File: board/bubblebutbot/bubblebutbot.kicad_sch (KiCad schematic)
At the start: 15 parts, among them J1 Screw_Terminal_01x02, J2 Screw_Terminal_01x02, J3 Conn_01x06_Female, J4 Conn_01x06_Female, Q1 FDN336P, U1 WeMos_D1_mini, U2 18350-HOLDER, U3 TPS613222ADBV

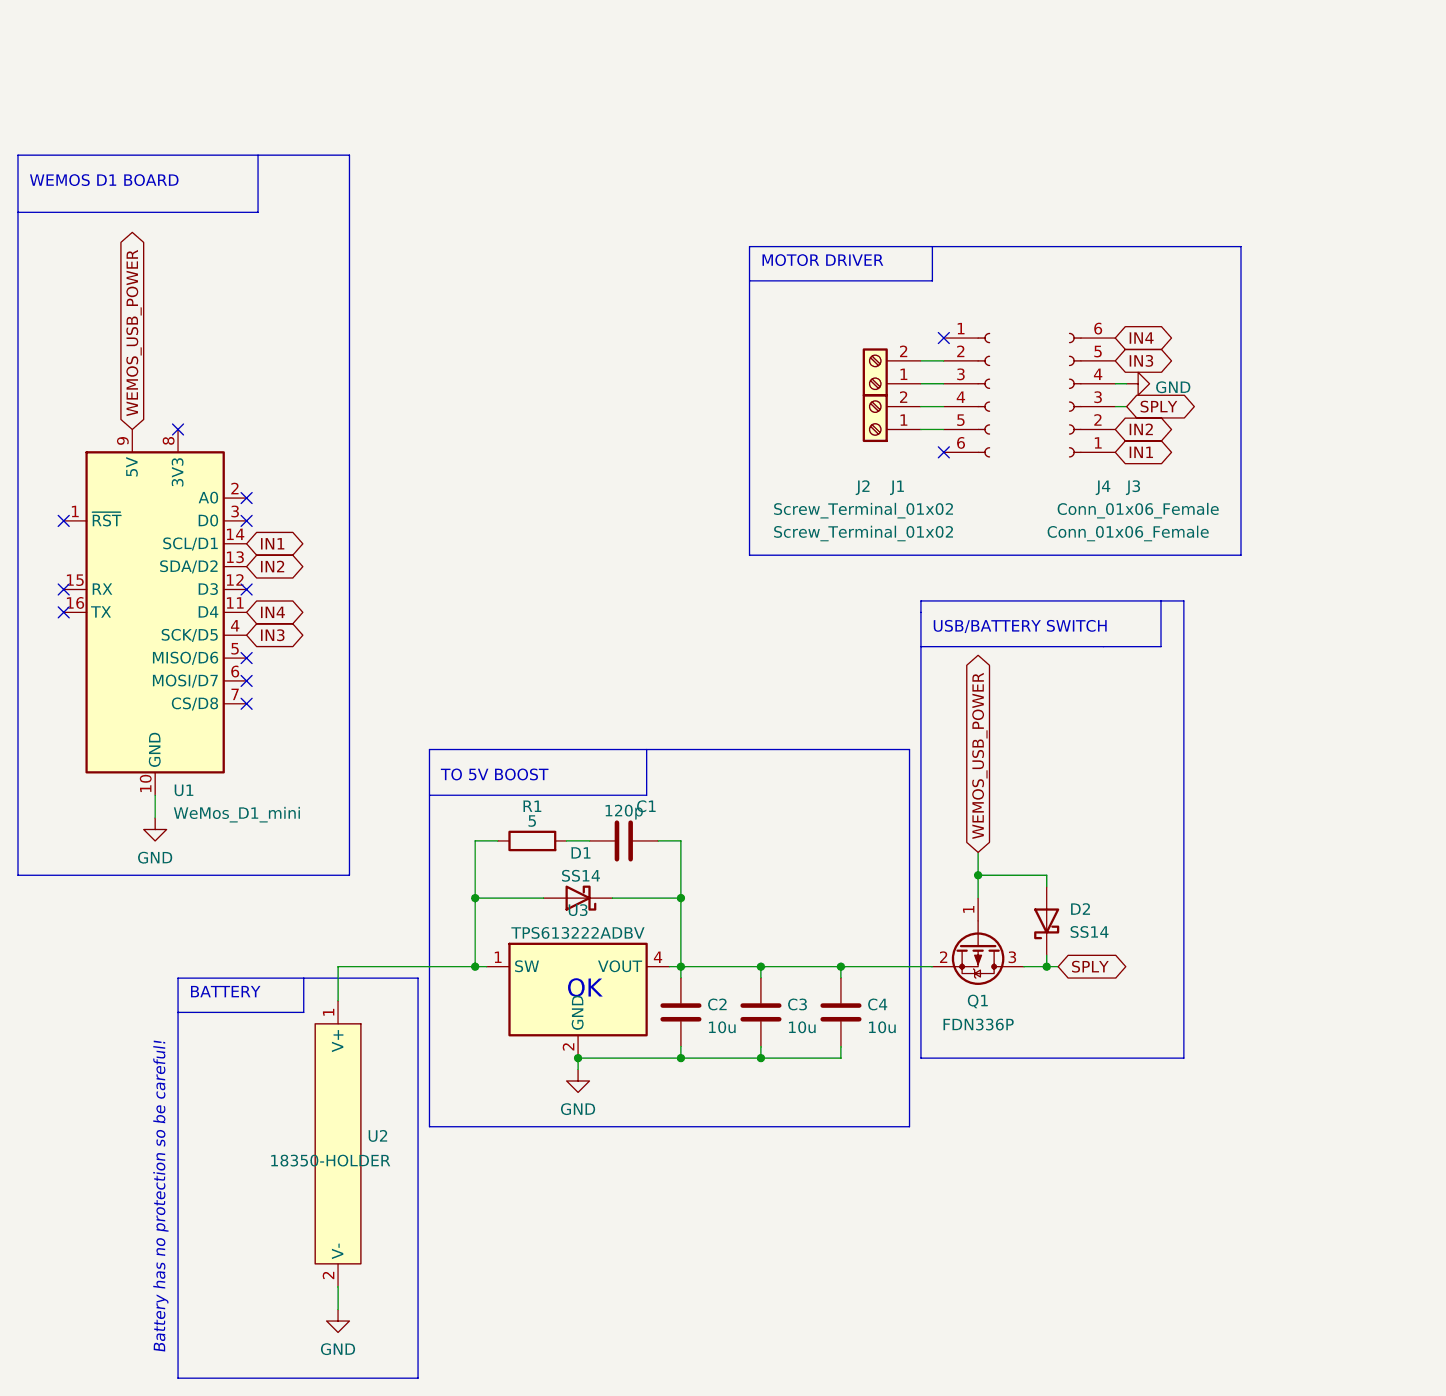
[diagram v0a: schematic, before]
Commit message: Finished prototype pcb
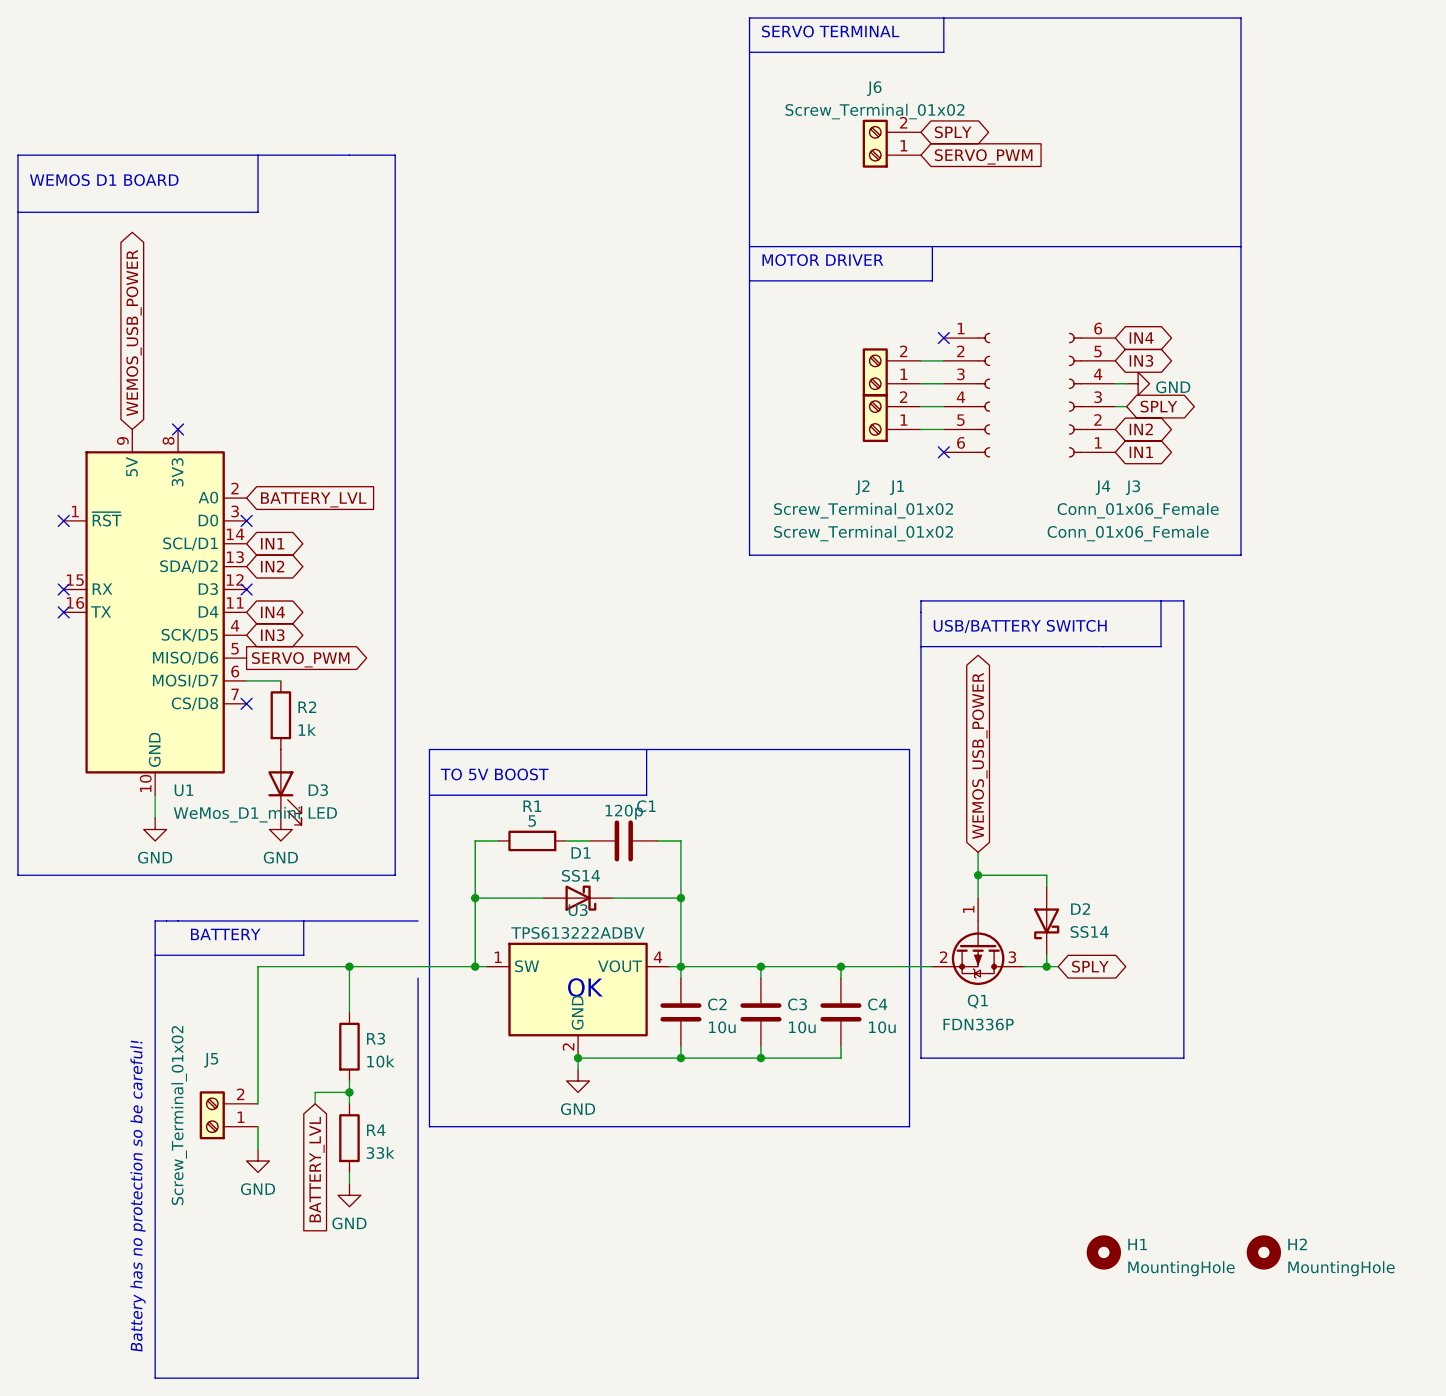
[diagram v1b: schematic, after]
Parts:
- removed U2: 18350-HOLDER, CustomFootprints:18350-Holder, symbol CustomSymbols:18350-HOLDER
- added D3: LED, LED_SMD:LED_0603_1608Metric_Pad1.05x0.95mm_HandSolder, symbol Device:LED
- added H1, H2: MountingHole, MountingHole:MountingHole_3.2mm_M3_ISO14580_Pad, symbol Mechanical:MountingHole
- added J5, J6: Screw_Terminal_01x02, TerminalBlock:TerminalBlock_bornier-2_P5.08mm, symbol Connector:Screw_Terminal_01x02
- added R2: 1k, Resistor_SMD:R_0603_1608Metric_Pad0.98x0.95mm_HandSolder, symbol Device:R
- added R3: 10k, Resistor_SMD:R_0603_1608Metric_Pad0.98x0.95mm_HandSolder, symbol Device:R
- added R4: 33k, Resistor_SMD:R_0603_1608Metric_Pad0.98x0.95mm_HandSolder, symbol Device:R
- J1, J2: LCSC (none) -> C8475
- J3, J4: LCSC (none) -> C350307
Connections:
- net GND: now also D3.1 (K), J5.1 (Pin_1), R4.2
- net SPLY: now also J6.2 (Pin_2)
- net at D1.2 (A), R1.1, U3.1 (SW): now also J5.2 (Pin_2), R3.1
- net BATTERY_LVL: now reaches U1.2 (A0)
- net BATTERY_LVL: now also R3.2, R4.1
- net SERVO_PWM: now reaches U1.5 (MISO/D6)
- net SERVO_PWM: now also J6.1 (Pin_1)
- net at U1.6 (MOSI/D7): now also R2.1
- new net: D3.2 (A), R2.2
- no-connect marks 12 -> 9
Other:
- note added: "SERVO TERMINAL"
